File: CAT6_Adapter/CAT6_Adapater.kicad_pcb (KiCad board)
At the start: 2 copper layers, 7 parts, among them J1 RJ45, J2 RJ45, P1 CONN_02X04, P2 CONN_01X02, U1 MCP2551-I/P

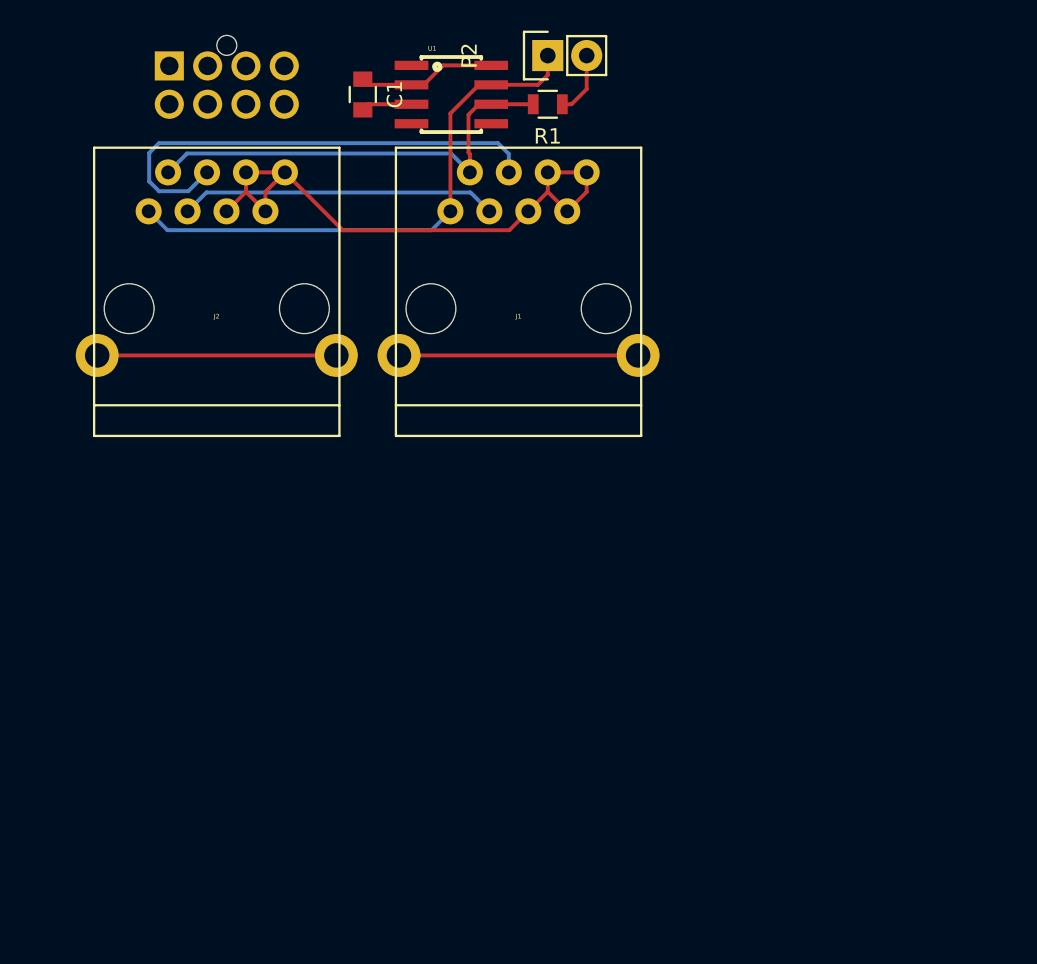
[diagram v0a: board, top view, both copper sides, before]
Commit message: CPL and CAT6 Adapter
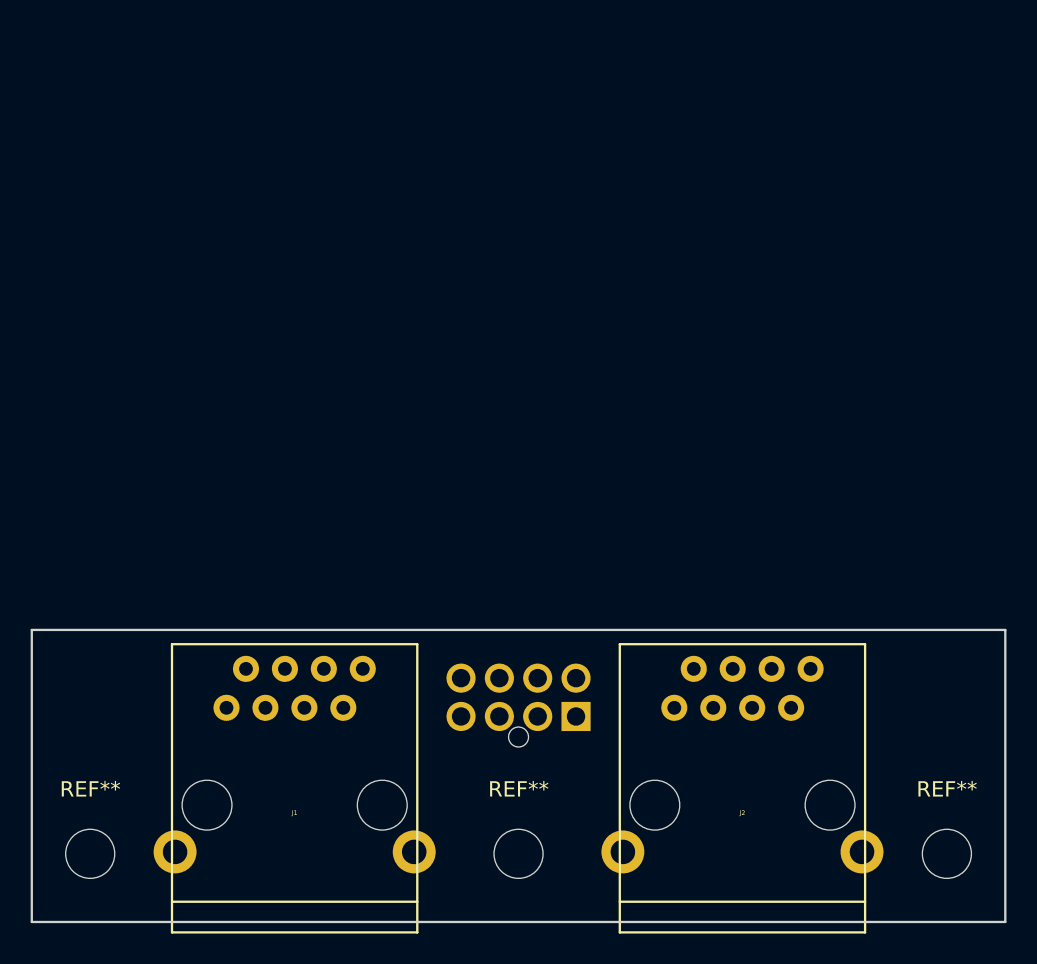
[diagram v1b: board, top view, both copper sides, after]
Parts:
- removed C1: 10uF, Capacitors_SMD:C_0805
- removed P2: CONN_01X02, Pin_Headers:Pin_Header_Straight_1x02
- removed R1: R, Resistors_SMD:R_0805
- removed U1: MCP2551-I/P, UNCAMotorsports:SOIC-8
- added REF**: MountingHole_3.2mm_M3, Mounting_Holes:MountingHole_3.2mm_M3, F.Cu at (107.3, 97.2)
- added REF**: MountingHole_3.2mm_M3, Mounting_Holes:MountingHole_3.2mm_M3, F.Cu at (163.2, 97.2)
- added REF**: MountingHole_3.2mm_M3, Mounting_Holes:MountingHole_3.2mm_M3, F.Cu at (135.3, 97.2)
- moved P1 50.0 mm to (139.0, 88.2), turned to 180 degrees
- moved J2 47.2 mm to (149.9, 94.0)
- moved J1 35.5 mm to (120.7, 94.0)
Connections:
- P1 pad 1: /CANTX -> /CANH
- P1 pad 2: +5V -> /RST1
- P1 pad 3: /CANRX -> /RST0
- P1 pad 4: GND -> /CANL
- P1 pad 5: /RST0 -> +12V
- P1 pad 7: /RST1 -> +12V
- P1 pad 8: GND -> +12V
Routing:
- net +12V: track 38.9 -> 0.00 mm
- net /CANH: track 35.7 -> 0.00 mm
- net /RST1: track 31.6 -> 0.00 mm
- net /CANL: track 29.0 -> 0.00 mm
- net /RST0: track 20.7 -> 0.00 mm
- net Net-(J2-Pad9): track 15.6 -> 0.00 mm
- net Net-(J1-Pad9): track 15.6 -> 0.00 mm
- net GND: track 9.06 -> 0.00 mm
- net Net-(P2-Pad2): track 4.19 -> 0.00 mm
- net +5V: track 3.33 -> 0.00 mm
- net /CANRX: track 0.80 -> 0.00 mm
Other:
- board outline added: 63.5 x 19 mm
